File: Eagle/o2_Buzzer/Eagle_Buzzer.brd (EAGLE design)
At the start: 24.2 x 20 mm, 7 parts, among them Q1 S9013

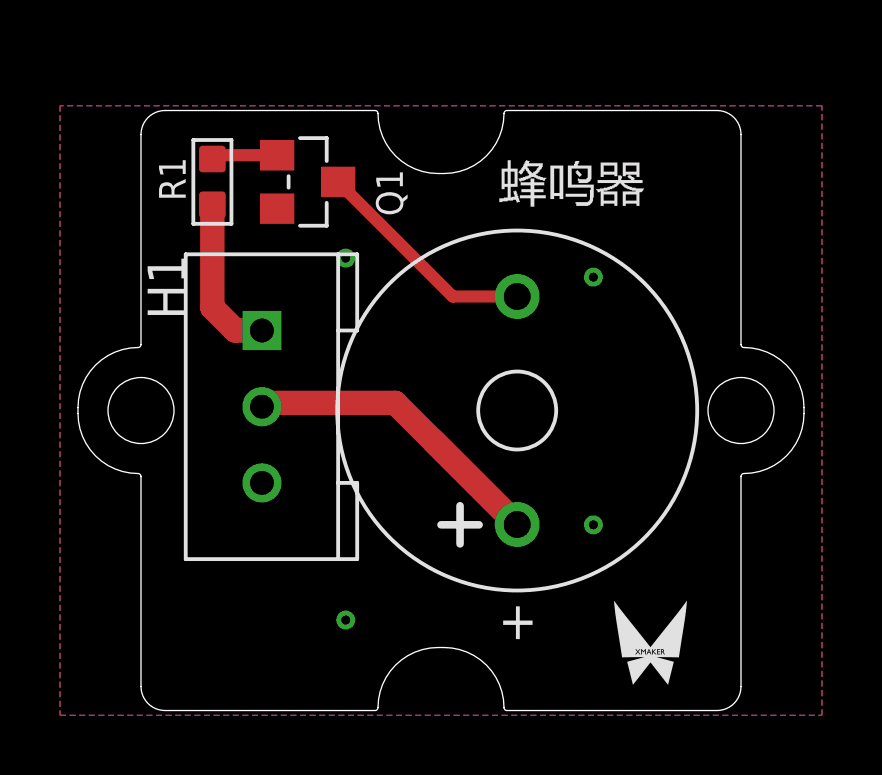
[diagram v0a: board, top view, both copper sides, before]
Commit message: 调整蜂鸣器
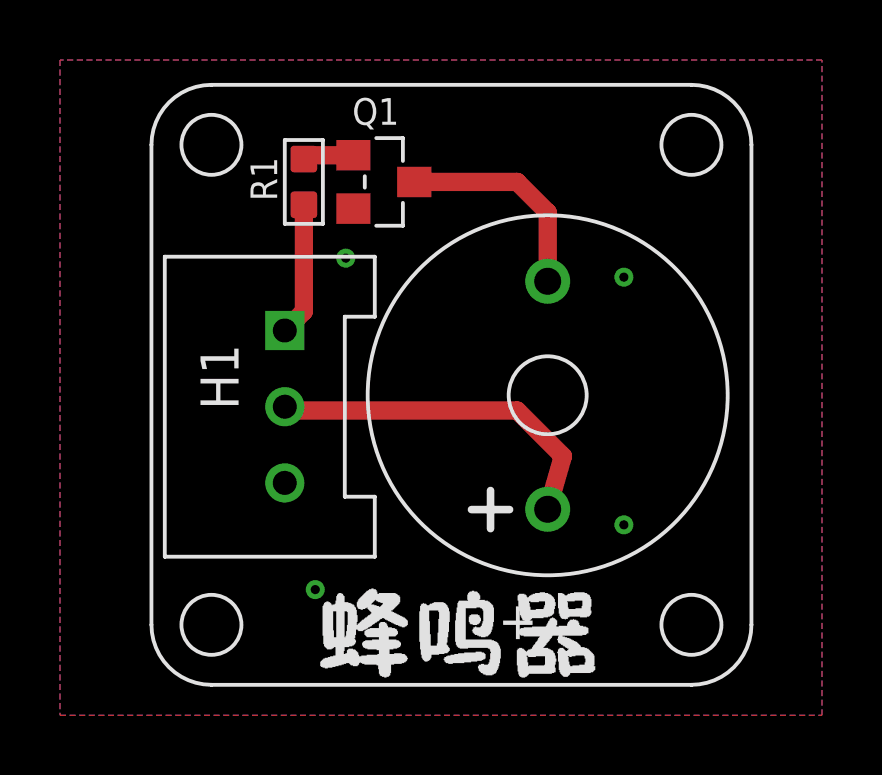
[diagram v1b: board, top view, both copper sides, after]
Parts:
- removed U$1: (no value), moudle:1U-DIM-W/-DRILL
- removed U$2: (no value), Logo:OSHW_FILLX200_NOTEXT
- removed U$3: (no value), switch-tact:XMAKERLOGO
- added U$4: DIMENSION_2MM2MM, Xmaker:DIMENSION_2MM*2MM
- added U$5: XMAKERLOGO_2.5MM_TOP, Xmaker:XMAKERLOGO_2.5MM_TOP
- added U$6: OPENHARDWARE_2.5MM_TOP, Xmaker:OPENSOURCELOGO_2.5MM
- added U$7: NAME_BUZZER, Xmaker:NAME_BUZZER
- H1: value HEAD_LOCK -> HEAD_LOCK_3PIN_2; device HEAD_LOCK:HEAD_LOCK -> Xmaker:HEAD_LOCK_3PIN_2
- moved R1 3.05 mm to (-4.57, 7.62)
- moved H1 2.65 mm to (-5.21, 0.13), turned to 0 degrees
- moved Q1 2.54 mm to (-1.91, 7.62)
- moved BUZ1 1.14 mm to (3.56, 0.51)
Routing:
- net VCC: track 14.2 -> 11.8 mm
- net D1: track 5.40 -> 4.45 mm
- net N$2: track 2.29 -> 1.70 mm
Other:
- board outline removed
- board text removed: "GND"
- board text removed: "SIG"
- board text removed: "VCC"

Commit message: a
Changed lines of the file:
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@@
 <plain>
 <text x="1.905" y="-7.62" size="1.27" layer="21" ratio="12">+</text>
-<text x="5.715" y="-8.255" size="1.27" layer="22" ratio="12" rot="MR0">Buzzer</text>
+<text x="3.175" y="-8.255" size="1.27" layer="22" ratio="12" rot="MR0">Buzzer</text>
 </plain>
 <attributes>
@@
 <attribute name="VALUE" x="11.811" y="-3.937" size="1.778" layer="27" ratio="10" rot="R90"/>
 </element>
-<element name="H1" library="Xmaker" package="HEAD_LOCK_3PIN_2" value="HEAD_LOCK_3PIN_2" x="-5.207" y="0.127"/>
+<element name="H1" library="Xmaker" package="HEAD_LOCK_3PIN_2" value="HEAD_LOCK_3PIN_2" x="-5.207" y="0.127" smashed="yes">
+<attribute name="NAME" x="-8.811" y="5.699" size="1.27" layer="21"/>
+</element>
 <element name="U$4" library="Xmaker" package="DIMENSION_2MM*2MM" value="DIMENSION_2MM2MM" x="-9.652" y="-9.144"/>
 <element name="U$5" library="Xmaker" package="XMAKERLOGO_2.5MM_TOP" value="XMAKERLOGO_2.5MM_TOP" x="-1.016" y="8.128" rot="MR180"/>
